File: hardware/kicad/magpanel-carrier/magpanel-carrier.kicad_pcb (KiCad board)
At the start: 2 copper layers, 100 x 63.5 mm, 38 parts, among them J1 5V IN, J10 EXP, J2 HUB75E PANEL 1, J3 HUB75E PANEL 2, J4 HUB75E PANEL 3, J5 LDR, J6 MIC, J7 ENC, J8 DHT, J9 TOUCH, U1 ESP32-S3-DevKitC-1, U2 74AHCT245, U3 74AHCT245

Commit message: Hardware: fit the KiCad carrier to the parts on hand
- Level shifters are CD74HCT245E in DIP-20 now (socketed footprint),
  stacked in one column with the A pins on the DevKit pin pitch
- DevKit right socket row is 1.0in (25.4 mm): the N16R8 clone on hand
  seated there in the 1:1 paper test; DEVKIT_RIGHT_ROWS switches back
  to the official 0.9in board
- Sensor headers follow the printed pin order of the JSUMO modules.
  The LDR and microphone modules are digital-only: LDR DO -> IO1,
  MIC OUT -> IO42, and R7 pulls the unused analog mic input IO2 to GND
- The 5 V trunk runs below the buffers and enters the DevKit 5V pin
  from underneath the module
- The fab stage also writes a 1:1 placement PDF with a 100 mm scale bar
- Wiring diagram (hardware/gen_schematic.py) and docs follow the actual
  module pinouts

ERC 0, DRC 0 violations, 0 unconnected items, 0 schematic parity issues.

Co-Authored-By: Claude Opus 5.5 <noreply@anthropic.com>
Claude-Session: https://claude.ai/code/session_01CdkdNf8EcXy8Er9VmQyghz
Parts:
- added R7: 100k, Resistor_SMD:R_0805_2012Metric, F.Cu at (128.0, 61.8)
- J6: footprint Connector_PinHeader_2.54mm:PinHeader_1x04_P2.54mm_Vertical -> Connector_PinHeader_2.54mm:PinHeader_1x03_P2.54mm_Vertical
- U2, U3: value 74AHCT245 -> 74HCT245; footprint Package_SO:SOIC-20W_7.5x12.8mm_P1.27mm -> Package_DIP:DIP-20_W7.62mm_Socket
- moved U3 16.0 mm to (101.0, 104.9)
- moved C8 10.6 mm to (90.0, 107.6), turned to 180 degrees
- moved U2 10.2 mm to (101.0, 77.0)
- moved C4 7.47 mm to (90.0, 104.9), turned to 180 degrees
- moved RN1 6.35 mm to (87.6, 58.0)
- moved RN4 5.08 mm to (87.6, 96.0)
- moved C3 2.59 mm to (90.0, 77.0), turned to 180 degrees
- moved C5 2.54 mm to (128.0, 66.8)
- moved C6 2.54 mm to (128.0, 69.4)
- moved C7 2.54 mm to (128.0, 71.9)
- moved R6 2.54 mm to (128.0, 92.2)
- moved RN2 1.29 mm to (87.6, 68.1)
- moved RN3 0.20 mm to (87.6, 85.9)
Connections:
- net /LDR_AO renamed /LDR_OUT
- J6 pad 1: /MIC_AO -> /MIC_DO
- J8 pad 1: +3V3 -> GND
- J8 pad 3: GND -> +3V3
- J9 pad 1: GND -> /TOUCH_OUT
- J9 pad 3: /TOUCH_OUT -> GND
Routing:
- net +5V: track 119.1 -> 146.8 mm
- net /HUB_ADDR_C: track 67.9 -> 41.9 mm, vias 2 -> 0
- net GND: track 382.8 -> 398.8 mm
- net +3V3: track 146.4 -> 132.6 mm
- net /MIC_AO: track 14.3 -> 2.99 mm
- net /MIC_DO: track 19.4 -> 10.0 mm
- net /HUB_LAT3: track 16.3 -> 21.8 mm
- net /HUB_R2: track 37.6 -> 41.6 mm
- net /HUB_ADDR_E: track 50.4 -> 54.0 mm, vias 1 -> 0
- net /HUB_B1: track 34.0 -> 37.2 mm, vias 1 -> 0
- net /R2_5V: track 3.34 -> 5.96 mm
- net /R1_5V: track 3.34 -> 5.96 mm
- net /OE_5V: track 3.34 -> 5.96 mm
- net /LAT_5V: track 3.34 -> 5.96 mm
- net /LAT3_5V: track 3.34 -> 5.96 mm
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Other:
- board text added: "Carrier v1.1"
- board text added: "MagPanel"
- board text added: "MagPanel Carrier v1.1 2026-10-02 github.com/Kem4lk/magpanel"
- board text removed: "AO"
- board text removed: "MagPanel Carrier v1.0"
- board text removed: "github.com/Kem4lk/magpanel"

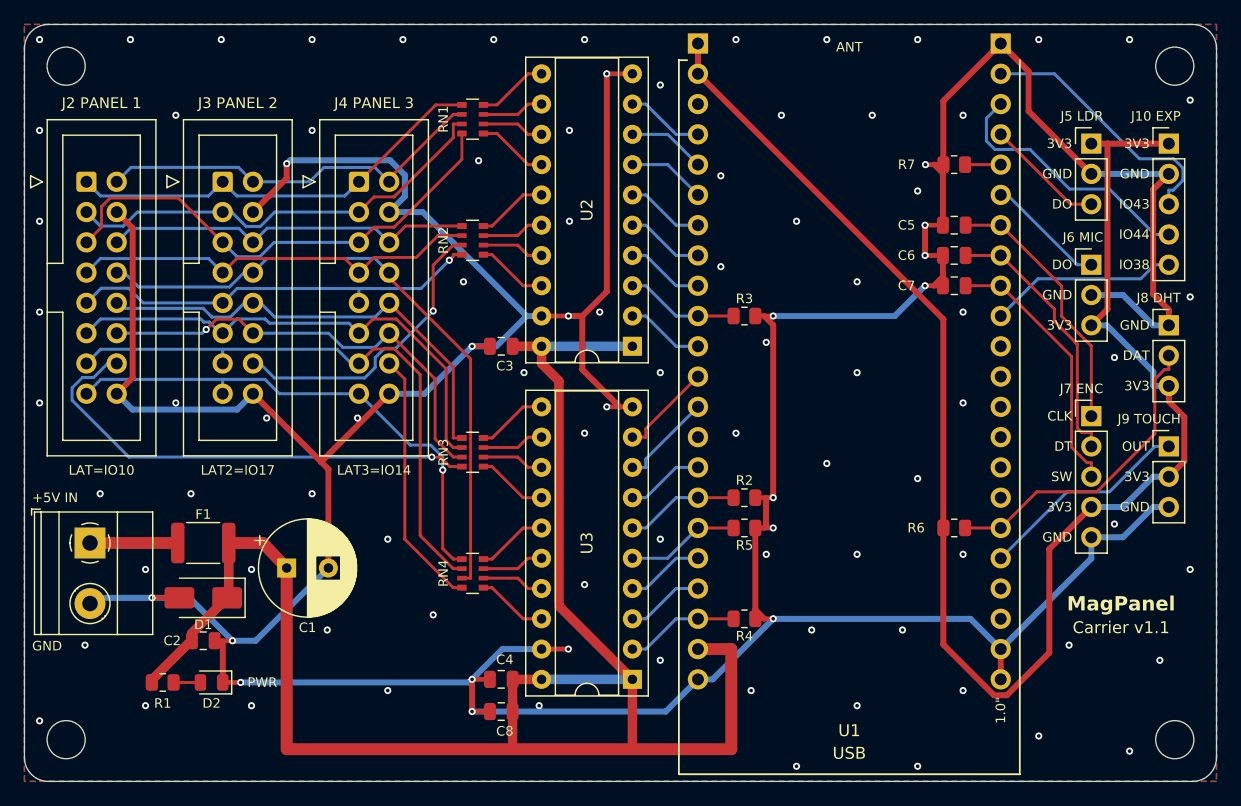
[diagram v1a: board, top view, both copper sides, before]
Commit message: Hardware: make the KiCad carrier hand-solder friendly (v1.2)
- Replace the four 4x0603 resistor arrays (0.35 mm between pads) with
  16 discrete 0805 33R resistors (R10-R25) in one column, each in line
  with its 74HCT245 B pin (1.14 mm between neighbouring pads).
- Use HandSolder footprints for every SMD part and LongPads DIP sockets.
- Add a 0.5 mm courtyard clearance DRC rule. v1.1 had 13 violations
  (tightest 0.16 mm); v1.2 has none (tightest 0.58 mm).
- Widen the gaps between the HUB75 box headers from 2.4 mm to 3.8 mm and
  move the SMD parts under the DevKit 4.5 mm away from the socket rows.
- Re-lay the 5 V input block; tie the TVS anode straight to the input
  GND with a locked wide track.
- Seed KiCad's UUID generator so regenerated files are reproducible.
- Document the assembly order and the first power-on check.

Co-Authored-By: Claude Opus 5.5 <noreply@anthropic.com>
Claude-Session: https://claude.ai/code/session_01CdkdNf8EcXy8Er9VmQyghz
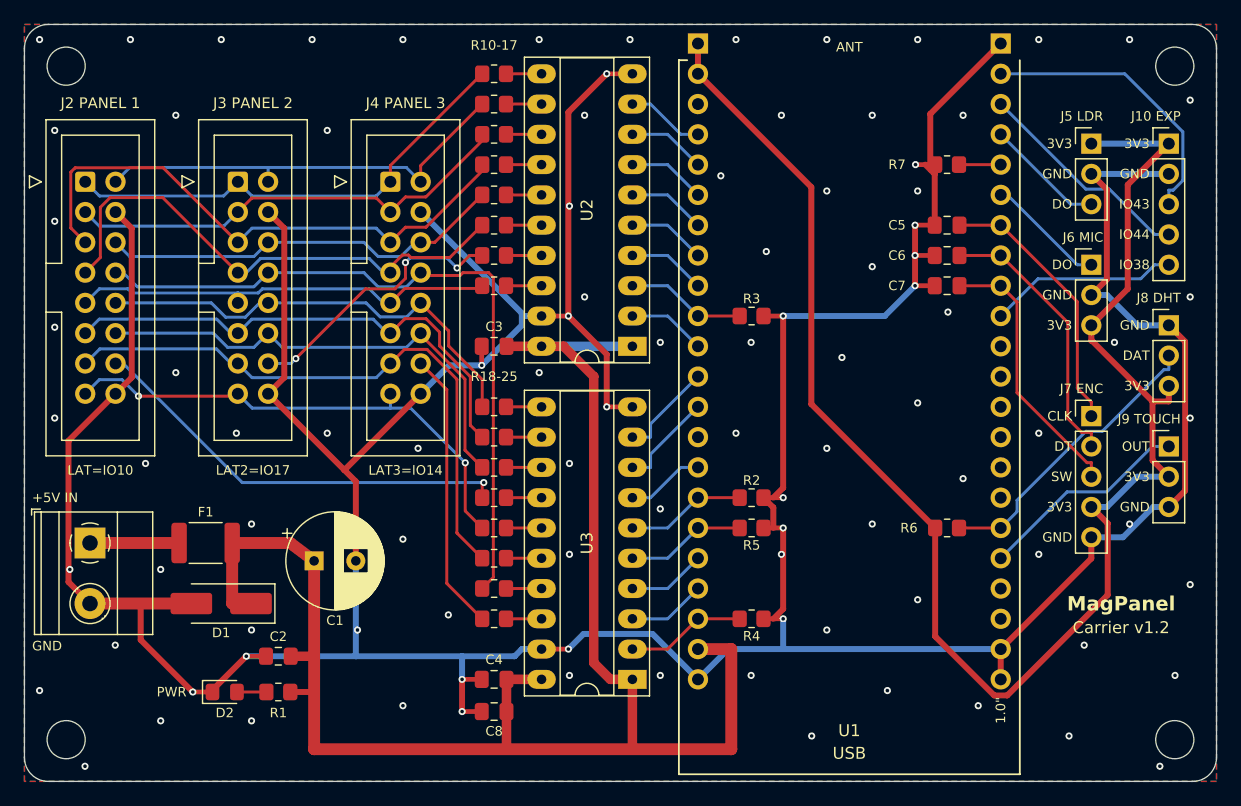
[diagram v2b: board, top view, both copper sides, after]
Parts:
- removed RN1, RN2, RN3, RN4: 4x33R, Resistor_SMD:R_Array_Convex_4x0603
- added R10: 33R, Resistor_SMD:R_0805_2012Metric_Pad1.20x1.40mm_HandSolder, F.Cu at (89.4, 54.1)
- added R11: 33R, Resistor_SMD:R_0805_2012Metric_Pad1.20x1.40mm_HandSolder, F.Cu at (89.4, 56.7)
- added R12: 33R, Resistor_SMD:R_0805_2012Metric_Pad1.20x1.40mm_HandSolder, F.Cu at (89.4, 59.2)
- added R13: 33R, Resistor_SMD:R_0805_2012Metric_Pad1.20x1.40mm_HandSolder, F.Cu at (89.4, 61.8)
- added R14: 33R, Resistor_SMD:R_0805_2012Metric_Pad1.20x1.40mm_HandSolder, F.Cu at (89.4, 64.3)
- added R15: 33R, Resistor_SMD:R_0805_2012Metric_Pad1.20x1.40mm_HandSolder, F.Cu at (89.4, 66.8)
- added R16: 33R, Resistor_SMD:R_0805_2012Metric_Pad1.20x1.40mm_HandSolder, F.Cu at (89.4, 69.4)
- added R17: 33R, Resistor_SMD:R_0805_2012Metric_Pad1.20x1.40mm_HandSolder, F.Cu at (89.4, 71.9)
- added R18: 33R, Resistor_SMD:R_0805_2012Metric_Pad1.20x1.40mm_HandSolder, F.Cu at (89.4, 82.1)
- added R19: 33R, Resistor_SMD:R_0805_2012Metric_Pad1.20x1.40mm_HandSolder, F.Cu at (89.4, 84.6)
- added R20: 33R, Resistor_SMD:R_0805_2012Metric_Pad1.20x1.40mm_HandSolder, F.Cu at (89.4, 87.2)
- added R21: 33R, Resistor_SMD:R_0805_2012Metric_Pad1.20x1.40mm_HandSolder, F.Cu at (89.4, 89.7)
- added R22: 33R, Resistor_SMD:R_0805_2012Metric_Pad1.20x1.40mm_HandSolder, F.Cu at (89.4, 92.2)
- added R23: 33R, Resistor_SMD:R_0805_2012Metric_Pad1.20x1.40mm_HandSolder, F.Cu at (89.4, 94.8)
- added R24: 33R, Resistor_SMD:R_0805_2012Metric_Pad1.20x1.40mm_HandSolder, F.Cu at (89.4, 97.3)
- added R25: 33R, Resistor_SMD:R_0805_2012Metric_Pad1.20x1.40mm_HandSolder, F.Cu at (89.4, 99.9)
- C2, C3, C4, C5, C6, C7, C8: footprint Capacitor_SMD:C_0805_2012Metric -> Capacitor_SMD:C_0805_2012Metric_Pad1.18x1.45mm_HandSolder
- D1: footprint Diode_SMD:D_SMA -> Diode_SMD:D_SMA_Handsoldering
- D2: footprint LED_SMD:LED_0805_2012Metric -> LED_SMD:LED_0805_2012Metric_Pad1.15x1.40mm_HandSolder
- F1: footprint Fuse:Fuse_1812_4532Metric -> Fuse:Fuse_1812_4532Metric_Pad1.30x3.40mm_HandSolder
- R1, R2, R3, R4, R5, R6, R7: footprint Resistor_SMD:R_0805_2012Metric -> Resistor_SMD:R_0805_2012Metric_Pad1.20x1.40mm_HandSolder
- U2, U3: footprint Package_DIP:DIP-20_W7.62mm_Socket -> Package_DIP:DIP-20_W7.62mm_Socket_LongPads
- moved R1 9.73 mm to (71.3, 106.0), turned to 180 degrees
- moved C2 6.43 mm to (71.3, 103.0), turned to 180 degrees
- moved J4 2.64 mm to (80.7, 63.2)
- moved C1 2.38 mm to (74.3, 95.0)
- moved D1 1.57 mm to (66.5, 98.6)
- moved D2 1.36 mm to (66.8, 106.0), turned to 0 degrees
- moved J3 1.27 mm to (67.9, 63.2)
- moved C3 0.60 mm to (89.4, 77.0)
- moved C4 0.60 mm to (89.4, 104.9)
- moved C5 0.60 mm to (127.4, 66.8)
- moved C6 0.60 mm to (127.4, 69.4)
- moved C7 0.60 mm to (127.4, 71.9)
- moved C8 0.60 mm to (89.4, 107.6)
- moved R2 0.60 mm to (111.0, 89.7)
- moved R3 0.60 mm to (111.0, 74.5)
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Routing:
- net /HUB_B2: track 34.7 -> 44.1 mm
- net +5V: track 146.8 -> 138.5 mm
- net /HUB_ADDR_E: track 54.0 -> 60.5 mm
- net GND: track 398.8 -> 392.6 mm, vias 100 -> 98
- net /HUB_R2: track 41.6 -> 47.6 mm
- net /HUB_LAT: track 40.6 -> 36.4 mm
- net /HUB_R1: track 36.1 -> 39.8 mm
- net /EXP_IO44: track 22.1 -> 18.6 mm
- net +3V3: track 132.6 -> 136.0 mm
- net /HUB_G1: track 33.5 -> 36.5 mm
- net /R2_5V: track 5.96 -> 2.98 mm
- net /R1_5V: track 5.96 -> 2.98 mm
- net /OE_5V: track 5.96 -> 2.98 mm
- net /LAT_5V: track 5.96 -> 2.98 mm
- net /LAT3_5V: track 5.96 -> 2.98 mm
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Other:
- board text added: "Carrier v1.2"
- board text added: "MagPanel Carrier v1.2 2026-10-02 github.com/Kem4lk/magpanel"
- board text added: "R10-17"
- board text added: "R18-25"
- board text removed: "Carrier v1.1"
- board text removed: "MagPanel Carrier v1.1 2026-10-02 github.com/Kem4lk/magpanel"

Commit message: Hardware: use 10k for R7 so every SMD part is in Robotistan's stock
Robotistan's BOM check reported the 100k part (C17407, an LCSC "(SMT)"
listing) as out of stock. R7 only pulls the unused IO2 input low, so its
value does not matter. It now uses the same 10k part as R2-R6 and the
assembly BOM shrinks to 8 lines. Placement and copper are unchanged.

Also pin the creation time KiCad writes into gerber and drill files to
DATE, so the gerber zip only changes when the board does.

Co-Authored-By: Claude Opus 5.5 <noreply@anthropic.com>
Claude-Session: https://claude.ai/code/session_01CdkdNf8EcXy8Er9VmQyghz
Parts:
- R7: value 100k -> 10k
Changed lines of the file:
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@@
 			)
 		)
-		(property "Value" "100k"
+		(property "Value" "10k"
 			(at 0 1.65 180)
 			(layer "F.Fab")
